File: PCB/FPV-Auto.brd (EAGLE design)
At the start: 65.5 x 30 mm, 97 parts, among them Q310 CSD25402Q3A, Q320 BSS138, U100 ATMEGA328P-AU, U110 NRF24L01+_MINI, U120 74LVC2T45DCT, U140 DRV8835, U200 RASPBERRY_PI_ZERO_W_V1.1_GPIO, U210 MAX98357A, U300 BQ25892, U330 TPS61236P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

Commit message: Updated PCB
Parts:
- added U$3: (no value), FPV-Auto:HACKFFM_LOGO_STOP
- added U$9: (no value), FPV-Auto:DATE
- U200: value RASPBERRY_PI_ZERO_W_V1.1_GPIO -> RASPBERRY_PI_ZERO_W_V1.1_GPIO_DUAL; device FPV-Auto:RASPBERRY_PI_ZERO_W_V1.1_GPIO -> FPV-Auto:RASPBERRY_PI_ZERO_W_V1.1_GPIO_DUAL
- moved C212 8.13 mm to (63.8, 20.7), turned to 180 degrees
- moved C213 7.79 mm to (63.8, 22.5), turned to 180 degrees
- moved R300 6.30 mm to (11.1, 4.90), flipped to the bottom, turned to 90 degrees
- moved R210 5.37 mm to (48.9, 17.4), turned to 90 degrees
- moved U210 4.69 mm to (53.2, 18.2), turned to 90 degrees
- moved R211 4.39 mm to (46.9, 15.0)
- moved FB211 3.91 mm to (55.9, 21.3)
- moved C210 2.92 mm to (48.5, 21.1), turned to 90 degrees
- moved R320 2.85 mm to (8.80, 18.2), flipped to the bottom, turned to 0 degrees
- moved FB210 2.58 mm to (55.9, 22.9), turned to 180 degrees
- moved Q320 2.02 mm to (5.01, 17.6), flipped to the bottom, turned to 90 degrees
- moved C104 1.43 mm to (5.81, 20.8), flipped to the bottom, turned to 0 degrees
- moved C351 1.40 mm to (21.8, 19.4)
- moved R332 1.40 mm to (37.4, 21.2)
- moved R331 1.40 mm to (37.4, 18.3)
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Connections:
- removed net NRF_CE: U100.26, U110.3
- removed net NRF_MOSI: U100.23, U110.6
- removed net SCK/NRF_MISO: U100.17, U110.7, X100.3
- new net NRF_CS: U100.23, U110.3
- new net NRF_MISO: U100.26, U110.7
- new net SCK/NRF_MOSI: U100.17, U110.6, X100.3
- net +5V1: now also U200.SMD_2, U200.SMD_4; no longer U200.2, U200.4
- net BCLK: now also U200.SMD_12
- net DIN: now also U200.SMD_40; no longer U200.40
- net GND: now also U200.SMD_14, U200.SMD_20, U200.SMD_25, U200.SMD_30, U200.SMD_34, U200.SMD_39, U200.SMD_6, U200.SMD_9; no longer U200.39
- net LRCLK: now also U200.SMD_35
- net N$15: now also D320.2; no longer D320.1
- net N$18: now also D320.1; no longer D320.2
- net N$26: now also U200.SMD_8
- net N$27: now also U200.SMD_10
- net NRF_!CS: now also U100.24; no longer U100.25
- net NRF_SCK: now also U100.25; no longer U100.24
- net RASPI_DTR: now also U200.SMD_15
- net VO+: now also X210.1; no longer X210.2
- net VO-: now also X210.2; no longer X210.1
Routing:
- net SCK/NRF_MOSI: track 0.00 -> 35.8 mm, vias 0 -> 1
- net SCK/NRF_MISO: track 30.5 -> 0.00 mm
- net DIN: track 46.3 -> 21.5 mm, vias 0 -> 1
- net NRF_MISO: track 0.00 -> 22.2 mm
- net NRF_CE: track 20.8 -> 0.00 mm
- net NRF_CS: track 0.00 -> 20.5 mm
- net NRF_MOSI: track 20.4 -> 0.00 mm
- net N$19: track 3.41 -> 19.5 mm, vias 0 -> 1
- net RASPI_DTR: track 37.2 -> 47.4 mm, vias 0 -> 1
- net BCLK: track 37.6 -> 44.7 mm, vias 0 -> 1
- net GND: track 44.6 -> 38.9 mm, vias 108 -> 113
- net GAIN: track 2.82 -> 8.17 mm
- net LRCLK: track 14.9 -> 9.64 mm
- net N$15: track 18.7 -> 15.2 mm, vias 1 -> 0
- net DTR: track 4.95 -> 2.15 mm
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- added copper zone on layer 15, net GND
- added copper zone on layer 16, net INPUT
- removed copper zone on layer 1, net INPUT
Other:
- board size 65.5 x 30 mm -> 65.5 x 30.7 mm
- board text removed: "MotA MotB"
- board text removed: "Servo1 Servo2"

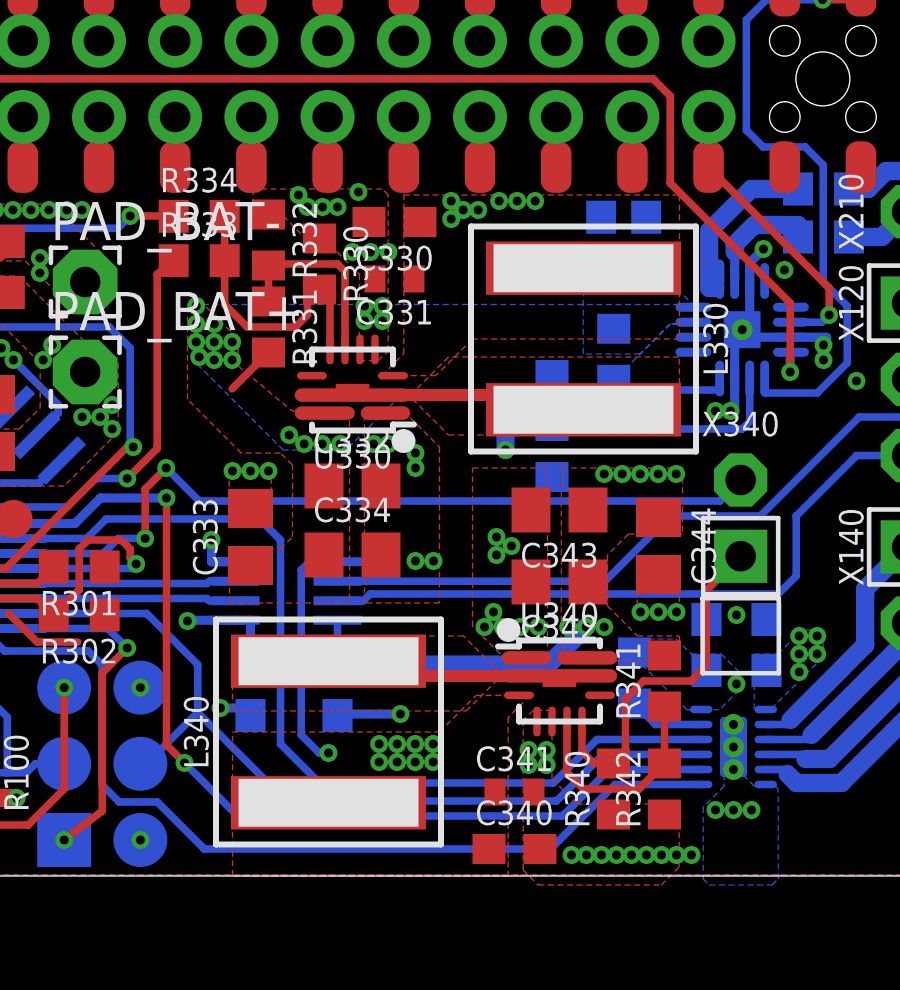
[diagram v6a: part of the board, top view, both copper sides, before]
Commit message: Board Layout Update
changed mask, changed 0402 caps -> 0603
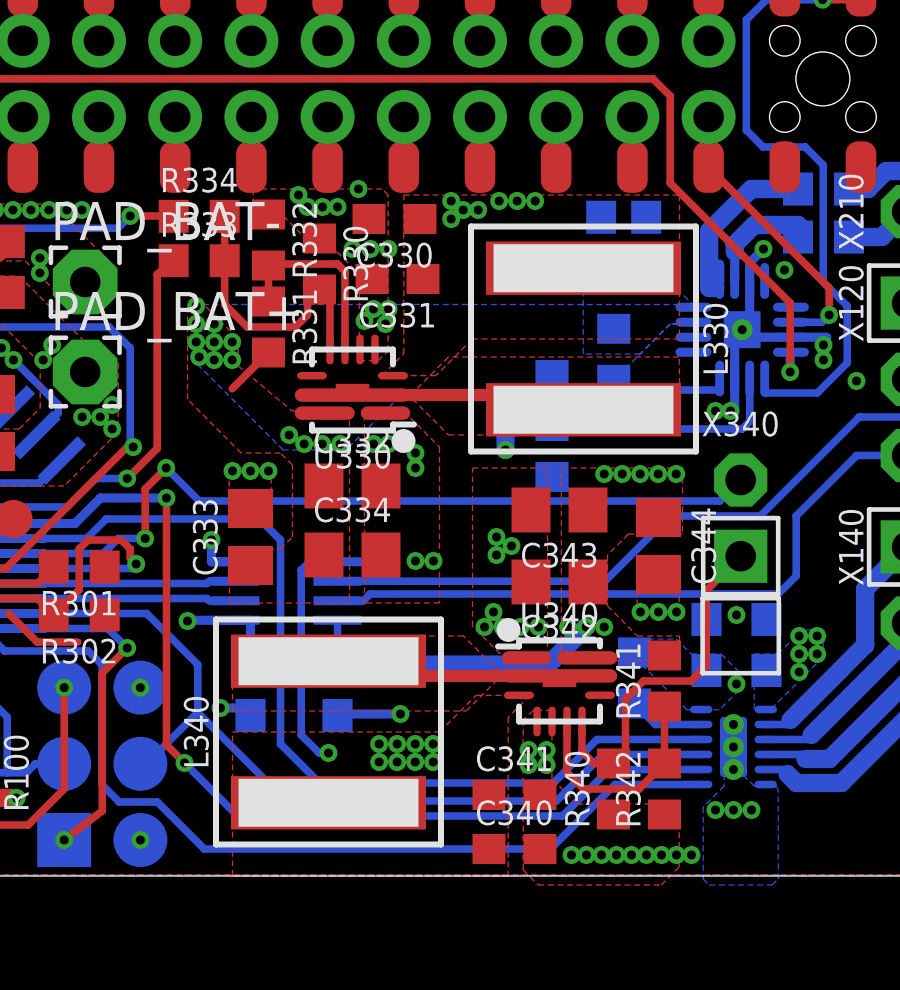
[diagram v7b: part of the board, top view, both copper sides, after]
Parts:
- C331, C341: device FPV-Auto:C0402 -> FPV-Auto:C0603
- moved C331 0.10 mm to (41.7, 19.9)
- moved C341 0.10 mm to (45.6, 2.70)
- moved C330 0.10 mm to (41.6, 21.9)
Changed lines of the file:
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@@
 <grid distance="0.5" unitdist="mm" unit="mm" style="lines" multiple="1" display="no" altdistance="0.1" altunitdist="mm" altunit="mm"/>
 <layers>
-<layer number="1" name="Top" color="4" fill="1" visible="no" active="yes"/>
+<layer number="1" name="Top" color="4" fill="1" visible="yes" active="yes"/>
 <layer number="2" name="GND" color="3" fill="1" visible="no" active="yes"/>
 <layer number="3" name="Route3" color="4" fill="3" visible="no" active="no"/>
 <layer number="14" name="Route14" color="1" fill="6" visible="no" active="no"/>
 <layer number="15" name="Route15" color="5" fill="1" visible="no" active="yes"/>
-<layer number="16" name="Bottom" color="1" fill="1" visible="yes" active="yes"/>
+<layer number="16" name="Bottom" color="1" fill="1" visible="no" active="yes"/>
 <layer number="17" name="Pads" color="2" fill="1" visible="yes" active="yes"/>
 <layer number="18" name="Vias" color="2" fill="1" visible="yes" active="yes"/>
@@
 <layer number="21" name="tPlace" color="7" fill="1" visible="no" active="yes"/>
 <layer number="22" name="bPlace" color="7" fill="1" visible="no" active="yes"/>
-<layer number="23" name="tOrigins" color="15" fill="1" visible="no" active="yes"/>
-<layer number="24" name="bOrigins" color="15" fill="1" visible="yes" active="yes"/>
+<layer number="23" name="tOrigins" color="15" fill="1" visible="yes" active="yes"/>
+<layer number="24" name="bOrigins" color="15" fill="1" visible="no" active="yes"/>
 <layer number="25" name="tNames" color="7" fill="1" visible="no" active="yes"/>
 <layer number="26" name="bNames" color="7" fill="1" visible="no" active="yes"/>
 <layer number="27" name="tValues" color="7" fill="1" visible="no" active="yes"/>
 <layer number="28" name="bValues" color="7" fill="1" visible="no" active="yes"/>
-<layer number="29" name="tStop" color="7" fill="3" visible="no" active="yes"/>
-<layer number="30" name="bStop" color="7" fill="6" visible="yes" active="yes"/>
+<layer number="29" name="tStop" color="7" fill="3" visible="yes" active="yes"/>
+<layer number="30" name="bStop" color="7" fill="6" visible="no" active="yes"/>
 <layer number="31" name="tCream" color="7" fill="4" visible="no" active="yes"/>
 <layer number="32" name="bCream" color="7" fill="5" visible="no" active="yes"/>
@@
 </class>
 </classes>
-<designrules name="PCB-POOL Standard_ML4">
+<designrules name="PCB-POOL Standard_ML4 *">
 <description language="de">&lt;b&gt;EAGLE Design Rules Prototypen  für PCB-POOL(R)&lt;/b&gt;
 &lt;p&gt;
@@
 <param name="mlMinCreamFrame" value="0mil"/>
 <param name="mlMaxCreamFrame" value="0.2mm"/>
-<param name="mlViaStopLimit" value="0mil"/>
+<param name="mlViaStopLimit" value="0.3mm"/>
 <param name="srRoundness" value="0"/>
 <param name="srMinRoundness" value="0mil"/>
@@
 <element name="R332" library="FPV-Auto" package="R0603" value="324K" x="37.41" y="21.2" rot="R270"/>
 <element name="R330" library="FPV-Auto" package="R0603" value="1M" x="39.11" y="20.4" rot="R270"/>
-<element name="C331" library="FPV-Auto" package="C0402" value="1µF" x="41.61" y="19.9" rot="R180"/>
-<element name="C330" library="FPV-Auto" package="C0603" value="10µF" x="41.61" y="21.8" rot="R180"/>
+<element name="C331" library="FPV-Auto" package="C0603" value="1µF" x="41.71" y="19.9" rot="R180"/>
+<element name="C330" library="FPV-Auto" package="C0603" value="10µF" x="41.61" y="21.9" rot="R180"/>
 <element name="C332" library="FPV-Auto" package="C0805" value="22µF" x="40.21" y="13"/>
 <element name="C333" library="FPV-Auto" package="C0805" value="22µF" x="36.81" y="11.3" rot="R90"/>
@@
 <element name="R342" library="FPV-Auto" package="R0603" value="294K" x="50.61" y="2.9" rot="R90"/>
 <element name="R340" library="FPV-Auto" package="R0603" value="1M" x="48.91" y="2.9" rot="R90"/>
-<element name="C341" library="FPV-Auto" package="C0402" value="1µF" x="45.61" y="2.8"/>
+<element name="C341" library="FPV-Auto" package="C0603" value="1µF" x="45.61" y="2.7"/>
 <element name="C340" library="FPV-Auto" package="C0603" value="10µF" x="45.61" y="0.9"/>
 <element name="C342" library="FPV-Auto" package="C0805" value="22µF" x="47.11" y="9.8" rot="R180"/>
@@
 <contactref element="PAD_BAT-" pad="1"/>
 <contactref element="PAD_IN-" pad="1"/>
-<via x="40.21" y="20.8" extent="1-16" drill="0.3"/>
-<via x="40.81" y="20.8" extent="1-16" drill="0.3"/>
-<via x="41.21" y="18.5" extent="1-16" drill="0.3"/>
+<via x="40.21" y="20.9" extent="1-16" drill="0.3"/>
+<via x="40.81" y="20.9" extent="1-16" drill="0.3"/>
+<via x="41.31" y="18.4" extent="1-16" drill="0.3"/>
 <via x="40.61" y="18.5" extent="1-16" drill="0.3"/>
 <via x="39.71" y="22.3" extent="1-16" drill="0.3"/>
@@
 <via x="44.91" y="8.8" extent="1-16" drill="0.3"/>
 <via x="51.01" y="0.7" extent="1-16" drill="0.3"/>
-<via x="40.61" y="19" extent="1-16" drill="0.3"/>
+<via x="40.91" y="18.9" extent="1-16" drill="0.3"/>
 <polygon width="0.254" layer="2">
 <vertex x="0" y="30.04"/>
@@
 <wire x1="36.31" y1="10.475" x2="35.51" y2="10.475" width="0.3048" layer="16"/>
 <wire x1="35.51" y1="10.475" x2="35.51" y2="11.2" width="0.3048" layer="16"/>
-<via x="41.41" y="20.8" extent="1-16" drill="0.3"/>
+<via x="41.41" y="20.9" extent="1-16" drill="0.3"/>
 <via x="38.41" y="22.7" extent="1-16" drill="0.3"/>
-<via x="40.41" y="22.8" extent="1-16" drill="0.3"/>
+<via x="40.41" y="22.9" extent="1-16" drill="0.3"/>
 <via x="38.71" y="22.3" extent="1-16" drill="0.3"/>
 <wire x1="29.67" y1="14.7" x2="30.4" y2="15.43" width="0.254" layer="16"/>
@@
 <via x="53.51" y="2.2" extent="1-16" drill="0.3"/>
 <via x="53.01" y="8.7" extent="1-16" drill="0.3"/>
-<via x="41.21" y="19" extent="1-16" drill="0.3"/>
+<via x="41.41" y="18.9" extent="1-16" drill="0.3"/>
 <via x="46.68" y="4.2" extent="1-16" drill="0.3"/>
 <via x="46.08" y="3.7" extent="1-16" drill="0.3"/>

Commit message: Silkscreen and Schematic Docu updates
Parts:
- RT301: value (none) -> NTCS0603E3103FLT
- moved U$9 3.00 mm to (33.0, 30.2)
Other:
- board text added: "+"
- board text added: "-"
- board text added: "1"
- board text added: "5V5"
- board text added: "BTN"
- board text added: "FPV-Auto"
- board text added: "GND"
- board text added: "M1"
- board text added: "M2"
- board text added: "NTC"
- board text added: "PPM"
- board text added: "Pin1"
- board text added: "SPK"
- board text added: "V1.0"
- board text added: "hackffm.de/fpva"
- board text removed: "hackffm.de"
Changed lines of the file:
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@@
 <layers>
 <layer number="1" name="Top" color="4" fill="1" visible="yes" active="yes"/>
-<layer number="2" name="GND" color="3" fill="1" visible="no" active="yes"/>
+<layer number="2" name="GND" color="3" fill="1" visible="yes" active="yes"/>
 <layer number="3" name="Route3" color="4" fill="3" visible="no" active="no"/>
 <layer number="14" name="Route14" color="1" fill="6" visible="no" active="no"/>
-<layer number="15" name="Route15" color="5" fill="1" visible="no" active="yes"/>
-<layer number="16" name="Bottom" color="1" fill="1" visible="no" active="yes"/>
+<layer number="15" name="Route15" color="5" fill="1" visible="yes" active="yes"/>
+<layer number="16" name="Bottom" color="1" fill="1" visible="yes" active="yes"/>
 <layer number="17" name="Pads" color="2" fill="1" visible="yes" active="yes"/>
 <layer number="18" name="Vias" color="2" fill="1" visible="yes" active="yes"/>
@@
 <layer number="21" name="tPlace" color="7" fill="1" visible="no" active="yes"/>
 <layer number="22" name="bPlace" color="7" fill="1" visible="no" active="yes"/>
-<layer number="23" name="tOrigins" color="15" fill="1" visible="yes" active="yes"/>
+<layer number="23" name="tOrigins" color="15" fill="1" visible="no" active="yes"/>
 <layer number="24" name="bOrigins" color="15" fill="1" visible="no" active="yes"/>
 <layer number="25" name="tNames" color="7" fill="1" visible="no" active="yes"/>
@@
 <layer number="28" name="bValues" color="7" fill="1" visible="no" active="yes"/>
 <layer number="29" name="tStop" color="7" fill="3" visible="yes" active="yes"/>
-<layer number="30" name="bStop" color="7" fill="6" visible="no" active="yes"/>
-<layer number="31" name="tCream" color="7" fill="4" visible="no" active="yes"/>
-<layer number="32" name="bCream" color="7" fill="5" visible="no" active="yes"/>
+<layer number="30" name="bStop" color="7" fill="6" visible="yes" active="yes"/>
+<layer number="31" name="tCream" color="7" fill="4" visible="yes" active="yes"/>
+<layer number="32" name="bCream" color="7" fill="5" visible="yes" active="yes"/>
 <layer number="33" name="tFinish" color="6" fill="3" visible="no" active="yes"/>
 <layer number="34" name="bFinish" color="6" fill="6" visible="no" active="yes"/>
@@
 <wire x1="65.52" y1="30.68" x2="0" y2="30.68" width="0" layer="20"/>
 <wire x1="0" y1="30.68" x2="0" y2="0" width="0" layer="20"/>
-<text x="64.94" y="12.38" size="1.016" layer="30" font="vector" rot="MR90" align="top-center">Lutz Lisseck
+<text x="64.94" y="12.38" size="1.016" layer="30" font="vector" ratio="12" rot="MR90" align="top-center">Lutz Lisseck
 David Merges</text>
-<text x="48.5" y="30.2" size="1.016" layer="30" font="vector" rot="MR0" align="top-center">hackffm.de</text>
+<text x="47" y="30.2" size="1.016" layer="30" font="vector" ratio="10" rot="MR0" align="top-center">hackffm.de/fpva</text>
 <text x="64.02" y="22.14" size="1.016" layer="22" rot="MR270" align="top-center">Spkr</text>
 <wire x1="61.22" y1="18.04" x2="61.22" y2="17.64" width="0.2" layer="22"/>
@@
 <wire x1="61.22" y1="9.84" x2="61.22" y2="9.44" width="0.2" layer="22"/>
 <wire x1="58.72" y1="9.84" x2="58.72" y2="9.54" width="0.2" layer="22"/>
+<text x="7" y="24" size="1.016" layer="30" font="vector" ratio="12" rot="MR180">Pin1</text>
+<text x="7.9" y="6" size="1.016" layer="30" font="vector" ratio="12" rot="MR0">+</text>
+<text x="7.6" y="0.6" size="1.016" layer="30" font="vector" ratio="12" rot="MR0">-</text>
+<text x="16.8" y="19.6" size="0.8128" layer="30" font="vector" ratio="12" rot="MR270">NTC</text>
+<text x="12.6" y="20.1" size="0.8128" layer="30" font="vector" ratio="12" rot="MR90">BTN</text>
+<text x="30" y="15.1" size="0.8128" layer="29" font="vector" ratio="12">+</text>
+<text x="32.2" y="18.3" size="0.8128" layer="29" font="vector" ratio="12">-</text>
+<text x="8.5" y="0.5" size="0.8128" layer="29" font="vector" ratio="12">-</text>
+<text x="8.5" y="6.8" size="0.8128" layer="29" font="vector" ratio="12">+</text>
+<text x="7.2" y="23.7" size="1.016" layer="29" font="vector" ratio="12">1</text>
+<text x="62.8" y="21.8" size="0.8128" layer="29" font="vector" ratio="12">SPK</text>
+<text x="62.8" y="18.9" size="0.8128" layer="29" font="vector" ratio="12">GND</text>
+<text x="62.8" y="16.3" size="0.8128" layer="29" font="vector" ratio="12">5V5</text>
+<text x="62.8" y="13.8" size="0.8128" layer="29" font="vector" ratio="12">PPM</text>
+<text x="62.8" y="10.8" size="0.8128" layer="29" font="vector" ratio="12">M1</text>
+<text x="62.8" y="8.3" size="0.8128" layer="29" font="vector" ratio="12">M2</text>
+<text x="56" y="9" size="1.016" layer="29" font="vector" ratio="12" rot="R90">FPV-Auto</text>
+<text x="57.3" y="9" size="1.016" layer="29" font="vector" ratio="12" rot="R90">V1.0</text>
 </plain>
 <attributes>
@@
 <element name="D321" library="diode" package="SOT23" value="BAT54A" x="18.1" y="20.71" rot="R90"/>
 <element name="R350" library="FPV-Auto" package="R0603" value="10K" x="21.69" y="21.6"/>
-<element name="RT301" library="FPV-Auto" package="R0603" value="" x="16.5" y="18.3" rot="R270"/>
+<element name="RT301" library="FPV-Auto" package="R0603" value="NTCS0603E3103FLT" x="16.5" y="18.3" rot="R270"/>
 <element name="U140" library="FPV-Auto" package="DSS(WSON-12)" value="DRV8835" x="52.91" y="4.3" rot="MR0"/>
 <element name="R140" library="FPV-Auto" package="R0603" value="1K" x="49.61" y="6.6" rot="MR270"/>
@@
 </element>
 <element name="U$3" library="FPV-Auto" package="HACKFFM_LOGO_STOP" value="" x="54.5" y="1"/>
-<element name="U$9" library="FPV-Auto" package="DATE" value="" x="36" y="30.2" rot="MR180"/>
+<element name="U$9" library="FPV-Auto" package="DATE" value="" x="33" y="30.2" rot="MR180"/>
 </elements>
 <signals>
